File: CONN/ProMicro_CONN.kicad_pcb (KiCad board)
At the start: 2 copper layers, 17.8 x 30.5 mm, 19 parts, among them J1 AVR-JTAG-10, J2 UEXT_Host, J3 Display, SW1 reset, SW2 user

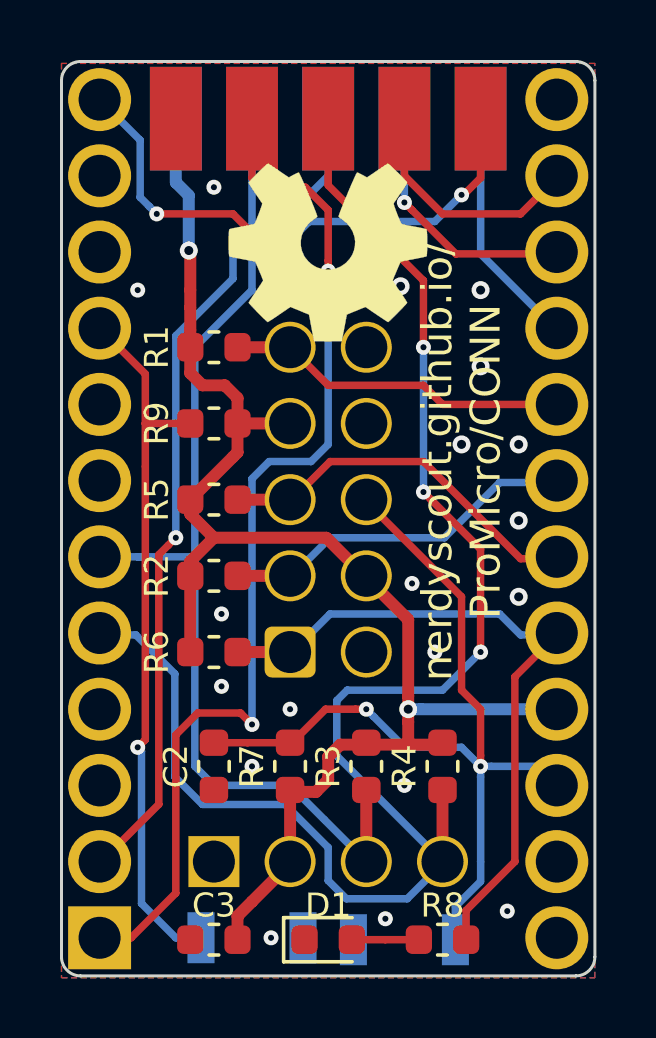
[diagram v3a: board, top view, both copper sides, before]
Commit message: update PCBs to be stackable
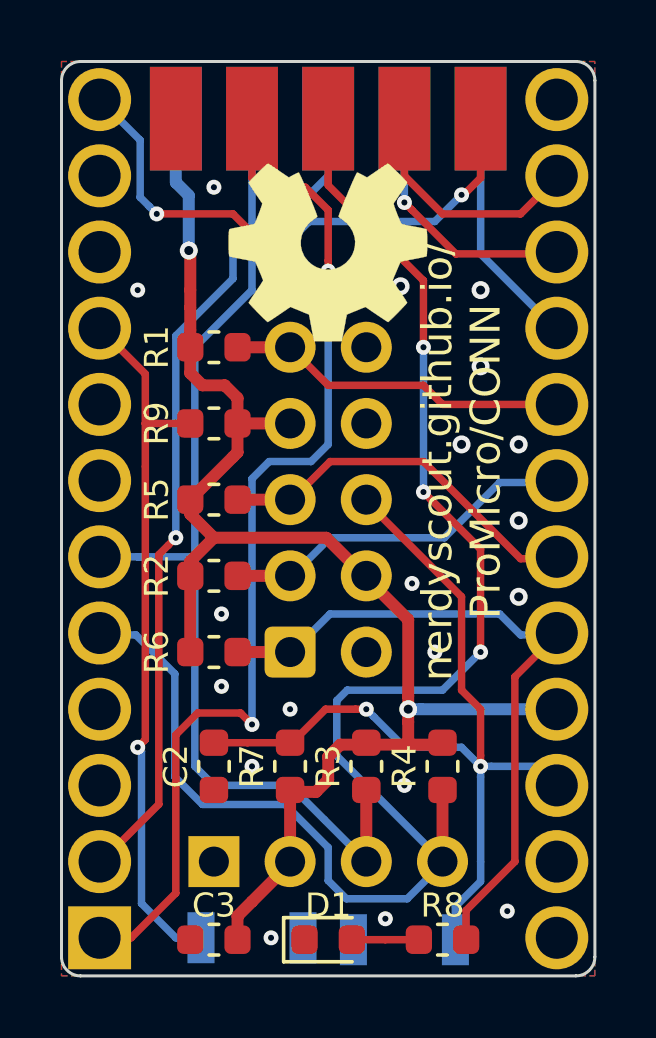
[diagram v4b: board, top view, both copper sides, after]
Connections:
- A1 pad 10: (no net) -> Net-(A1-Pad10)
- A1 pad 11: (no net) -> Net-(A1-Pad11)
- A1 pad 13: (no net) -> Net-(A1-Pad13)
- A1 pad 24: (no net) -> +5V
- A1 pad 7: (no net) -> Net-(A1-Pad7)
- A1 pad 8: (no net) -> Net-(A1-Pad8)
- J1 pad 8: (no net) -> Net-(J1-Pad8)
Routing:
- added copper zone on In2.Cu, net +3V3
- added copper zone on In1.Cu, net GND
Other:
- copper layers 2 -> 4
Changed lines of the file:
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@@
     (thickness 0.8)
     (drawings 9)
-    (tracks 229)
+    (tracks 228)
     (zones 0)
     (modules 19)
-    (nets 18)
+    (nets 25)
   )
   (page A4)
   (title_block
     (title ProMicro_CONN)
-    (date 2020-10-12)
-    (rev v1.3)
+    (date 2020-11-21)
+    (rev v1.4)
   )
   (layers
     (0 F.Cu mixed)
+    (1 In1.Cu signal)
+    (2 In2.Cu signal)
     (31 B.Cu mixed)
     (32 B.Adhes user)
@@
     (46 B.CrtYd user)
     (47 F.CrtYd user)
-    (48 B.Fab user hide)
-    (49 F.Fab user hide)
+    (48 B.Fab user)
+    (49 F.Fab user)
   )
   (setup
@@
     (mod_text_size 1 1)
     (mod_text_width 0.15)
-    (pad_size 1.524 1.524)
-    (pad_drill 0.762)
+    (pad_size 1.7 1.7)
+    (pad_drill 1)
     (pad_to_mask_clearance 0)
     (aux_axis_origin 137.16 104.14)
@@
   (net 16 CS1)
   (net 17 ~RST)
+  (net 18 "Net-(A1-Pad13)")
+  (net 19 "Net-(A1-Pad7)")
+  (net 20 "Net-(A1-Pad8)")
+  (net 21 "Net-(A1-Pad10)")
+  (net 22 "Net-(A1-Pad11)")
+  (net 23 +5V)
+  (net 24 "Net-(J1-Pad8)")
   (net_class Default "This is the default net class."
     (clearance 0.2)
@@
     (uvia_dia 0.3)
     (uvia_drill 0.1)
+    (add_net +5V)
     (add_net BTN)
     (add_net CIPO)
     (add_net COPI)
     (add_net CS1)
+    (add_net "Net-(A1-Pad10)")
+    (add_net "Net-(A1-Pad11)")
+    (add_net "Net-(A1-Pad13)")
+    (add_net "Net-(A1-Pad7)")
+    (add_net "Net-(A1-Pad8)")
     (add_net "Net-(D1-Pad2)")
+    (add_net "Net-(J1-Pad8)")
     (add_net RXD)
     (add_net SCK)
@@
     (pad 3 thru_hole circle (at 0 -5.08) (size 2.1 2.1) (drill 1.4) (layers *.Cu *.Mask)
       (net 1 GND))
-    (pad 13 thru_hole circle (at 15.24 -27.94) (size 2.1 2.1) (drill 1.4) (layers *.Cu *.Mask))
+    (pad 13 thru_hole circle (at 15.24 -27.94) (size 2.1 2.1) (drill 1.4) (layers *.Cu *.Mask)
+      (net 18 "Net-(A1-Pad13)"))
     (pad 4 thru_hole circle (at 0 -7.62) (size 2.1 2.1) (drill 1.4) (layers *.Cu *.Mask)
       (net 1 GND))
@@
     (pad 16 thru_hole circle (at 15.24 -20.32) (size 2.1 2.1) (drill 1.4) (layers *.Cu *.Mask)
       (net 10 SCK))
-    (pad 7 thru_hole circle (at 0 -15.24) (size 2.1 2.1) (drill 1.4) (layers *.Cu *.Mask))
+    (pad 7 thru_hole circle (at 0 -15.24) (size 2.1 2.1) (drill 1.4) (layers *.Cu *.Mask)
+      (net 19 "Net-(A1-Pad7)"))
     (pad 17 thru_hole circle (at 15.24 -17.78) (size 2.1 2.1) (drill 1.4) (layers *.Cu *.Mask)
       (net 11 TDI))
-    (pad 8 thru_hole circle (at 0 -17.78) (size 2.1 2.1) (drill 1.4) (layers *.Cu *.Mask))
+    (pad 8 thru_hole circle (at 0 -17.78) (size 2.1 2.1) (drill 1.4) (layers *.Cu *.Mask)
+      (net 20 "Net-(A1-Pad8)"))
     (pad 18 thru_hole circle (at 15.24 -15.24) (size 2.1 2.1) (drill 1.4) (layers *.Cu *.Mask)
       (net 12 TDO))
@@
     (pad 19 thru_hole circle (at 15.24 -12.7) (size 2.1 2.1) (drill 1.4) (layers *.Cu *.Mask)
       (net 14 TMS))
-    (pad 10 thru_hole circle (at 0 -22.86) (size 2.1 2.1) (drill 1.4) (layers *.Cu *.Mask))
+    (pad 10 thru_hole circle (at 0 -22.86) (size 2.1 2.1) (drill 1.4) (layers *.Cu *.Mask)
+      (net 21 "Net-(A1-Pad10)"))
     (pad 20 thru_hole circle (at 15.24 -10.16) (size 2.1 2.1) (drill 1.4) (layers *.Cu *.Mask)
       (net 15 TCK))
-    (pad 11 thru_hole circle (at 0 -25.4) (size 2.1 2.1) (drill 1.4) (layers *.Cu *.Mask))
+    (pad 11 thru_hole circle (at 0 -25.4) (size 2.1 2.1) (drill 1.4) (layers *.Cu *.Mask)
+      (net 22 "Net-(A1-Pad11)"))
     (pad 21 thru_hole circle (at 15.24 -7.62) (size 2.1 2.1) (drill 1.4) (layers *.Cu *.Mask)
       (net 2 +3V3))
@@
     (pad 23 thru_hole circle (at 15.24 -2.54) (size 2.1 2.1) (drill 1.4) (layers *.Cu *.Mask)
       (net 1 GND))
-    (pad 24 thru_hole circle (at 15.24 0) (size 2.1 2.1) (drill 1.4) (layers *.Cu *.Mask))
+    (pad 24 thru_hole circle (at 15.24 0) (size 2.1 2.1) (drill 1.4) (layers *.Cu *.Mask)
+      (net 23 +5V))
     (model ${KISYS3DMOD}/Module.3dshapes/Sparkfun_Pro_Micro.wrl
       (at (xyz 0 0 0))
@@
     (fp_line (start -2.18 5.1) (end 5.72 5.1) (layer B.Fab) (width 0.1))
     (fp_line (start -3.18 4.1) (end -2.18 5.1) (layer B.Fab) (width 0.1))
-    (pad 10 thru_hole circle (at 2.54 -10.16) (size 1.7 1.7) (drill 1.4) (layers *.Cu *.Mask)
+    (pad 10 thru_hole circle (at 2.54 -10.16) (size 1.7 1.7) (drill 1) (layers *.Cu *.Mask)
       (net 1 GND))
-    (pad 8 thru_hole circle (at 2.54 -7.62) (size 1.7 1.7) (drill 1.4) (layers *.Cu *.Mask))
-    (pad 6 thru_hole circle (at 2.54 -5.08) (size 1.7 1.7) (drill 1.4) (layers *.Cu *.Mask)
+    (pad 8 thru_hole circle (at 2.54 -7.62) (size 1.7 1.7) (drill 1) (layers *.Cu *.Mask)
+      (net 24 "Net-(J1-Pad8)"))
+    (pad 1 thru_hole circle (at 2.54 -5.08) (size 1.7 1.7) (drill 1) (layers *.Cu *.Mask)
       (net 17 ~RST))
-    (pad 4 thru_hole circle (at 2.54 -2.54) (size 1.7 1.7) (drill 1.4) (layers *.Cu *.Mask)
-      (net 2 +3V3))
-    (pad 2 thru_hole circle (at 2.54 0) (size 1.7 1.7) (drill 1.4) (layers *.Cu *.Mask)
+    (pad 4 thru_hole circle (at 2.54 -2.54) (size 1.7 1.7) (drill 1) (layers *.Cu *.Mask)
+      (net 2 +3V3))
+    (pad 2 thru_hole circle (at 2.54 0) (size 1.7 1.7) (drill 1) (layers *.Cu *.Mask)
       (net 1 GND))
-    (pad 9 thru_hole circle (at 0 -10.16) (size 1.7 1.7) (drill 1.4) (layers *.Cu *.Mask)
+    (pad 9 thru_hole circle (at 0 -10.16) (size 1.7 1.7) (drill 1) (layers *.Cu *.Mask)
       (net 11 TDI))
-    (pad 7 thru_hole circle (at 0 -7.62) (size 1.7 1.7) (drill 1.4) (layers *.Cu *.Mask)
-      (net 2 +3V3))
-    (pad 5 thru_hole circle (at 0 -5.08) (size 1.7 1.7) (drill 1.4) (layers *.Cu *.Mask)
+    (pad 1 thru_hole circle (at 0 -7.62) (size 1.7 1.7) (drill 1) (layers *.Cu *.Mask)
+      (net 2 +3V3))
+    (pad 5 thru_hole circle (at 0 -5.08) (size 1.7 1.7) (drill 1) (layers *.Cu *.Mask)
       (net 14 TMS))
-    (pad 3 thru_hole circle (at 0 -2.54) (size 1.7 1.7) (drill 1.4) (layers *.Cu *.Mask)
+    (pad 3 thru_hole circle (at 0 -2.54) (size 1.7 1.7) (drill 1) (layers *.Cu *.Mask)
       (net 12 TDO))
-    (pad 1 thru_hole roundrect (at 0 0) (size 1.7 1.7) (drill 1.4) (layers *.Cu *.Mask) (roundrect_rratio 0.147059)
+    (pad 1 thru_hole roundrect (at 0 0) (size 1.7 1.7) (drill 1) (layers *.Cu *.Mask) (roundrect_rratio 0.147)
       (net 15 TCK))
     (model ${KISYS3DMOD}/Connector_IDC.3dshapes/IDC-Header_2x05_P2.54mm_Vertical.wrl
@@
       (effects (font (size 0.8 0.8) (thickness 0.2)) (justify mirror))
     )
-    (pad 4 thru_hole circle (at 0 -7.62 270) (size 1.7 1.7) (drill 1.4) (layers *.Cu *.Mask)
+    (pad 4 thru_hole circle (at 0 -7.62 270) (size 1.7 1.7) (drill 1) (layers *.Cu *.Mask)
       (net 7 SDA))
-    (pad 3 thru_hole circle (at 0 -5.08 270) (size 1.7 1.7) (drill 1.4) (layers *.Cu *.Mask)
+    (pad 3 thru_hole circle (at 0 -5.08 270) (size 1.7 1.7) (drill 1) (layers *.Cu *.Mask)
       (net 9 SCL))
-    (pad 2 thru_hole circle (at 0 -2.54 270) (size 1.7 1.7) (drill 1.4) (layers *.Cu *.Mask)
-      (net 2 +3V3))
-    (pad 1 thru_hole rect (at 0 0 270) (size 1.7 1.7) (drill 1.4) (layers *.Cu *.Mask)
+    (pad 2 thru_hole circle (at 0 -2.54 270) (size 1.7 1.7) (drill 1) (layers *.Cu *.Mask)
+      (net 2 +3V3))
+    (pad 1 thru_hole rect (at 0 0 270) (size 1.7 1.7) (drill 1) (layers *.Cu *.Mask)
       (net 1 GND))
     (model ${KISYS3DMOD}/Connector_PinHeader_2.54mm.3dshapes/PinHeader_1x04_P2.54mm_Vertical.wrl
@@
   (segment (start 151.193452 80.01) (end 148.59 80.01) (width 0.25) (layer F.Cu) (net 6))
   (segment (start 148.59 99.275952) (end 148.59 101.663452) (width 0.4) (layer F.Cu) (net 7))
-  (segment (start 148.59 101.663452) (end 148.59 101.6) (width 0.25) (layer F.Cu) (net 7))
   (via (at 149.86 94.615) (size 0.5) (drill 0.2) (layers F.Cu B.Cu) (net 7))
   (via (at 147.955 84.455) (size 0.5) (drill 0.2) (layers F.Cu B.Cu) (net 7))
@@
     (polygon
       (pts
-        (xy 153.67 74.993452) (xy 135.89 74.993452) (xy 135.89 105.473452) (xy 153.67 105.473452)
+        (xy 153.67 74.93) (xy 135.89 74.93) (xy 135.89 105.41) (xy 153.67 105.41)
       )
     )
@@
     (polygon
       (pts
-        (xy 153.67 74.993452) (xy 135.89 74.993452) (xy 135.89 105.473452) (xy 153.67 105.473452)
+        (xy 153.67 74.93) (xy 135.89 74.93) (xy 135.89 105.41) (xy 153.67 105.41)
       )
     )
+  )
+  (zone (net 1) (net_name GND) (layer In1.Cu) (hatch edge 0.508)
+    (connect_pads (clearance 0.125))
+    (min_thickness 0.254)
+    (fill yes (arc_segments 32) (thermal_gap 0.508) (thermal_bridge_width 0.508))
+    (polygon
+      (pts
+        (xy 153.67 105.41) (xy 135.89 105.41) (xy 135.89 74.93) (xy 153.67 74.93)
+      )
+    )
+  )
+  (zone (net 2) (net_name +3V3) (layer In2.Cu) (hatch edge 0.508)
+    (connect_pads (clearance 0.125))
+    (min_thickness 0.254)
+    (fill yes (arc_segments 32) (thermal_gap 0.508) (thermal_bridge_width 0.508))
+    (polygon
+      (pts
+        (xy 153.67 105.41) (xy 135.89 105.41) (xy 135.89 74.93) (xy 153.67 74.93)
+      )
+    )
